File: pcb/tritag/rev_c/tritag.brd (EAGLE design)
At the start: 61 x 34.5 mm, 141 parts, among them J1 BAT_HOLE, J2 CON_MICRO_SDDM3AT-SF-PEJM5, J3 MICRO_USB_B_HIROSE_ZX62-B-5PA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, J4 TC2030-JLINK-NL, J5 TC2030-JLINK-NL, T1 HHM1595A1, U1 DW1000, U10 STM32F091CC, U2 FT232RQ, U3 LIS2DW12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

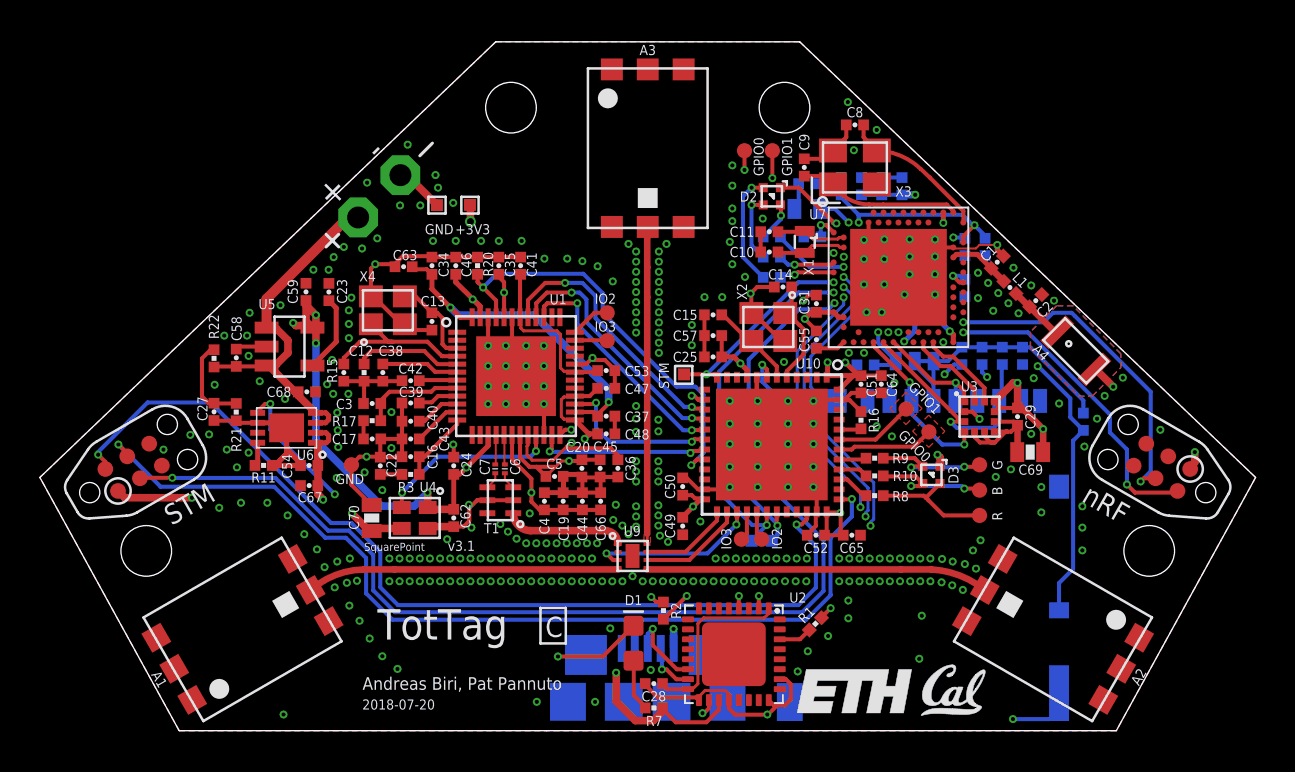
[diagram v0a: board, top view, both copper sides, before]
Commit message: added small fixes from Gerber inspection
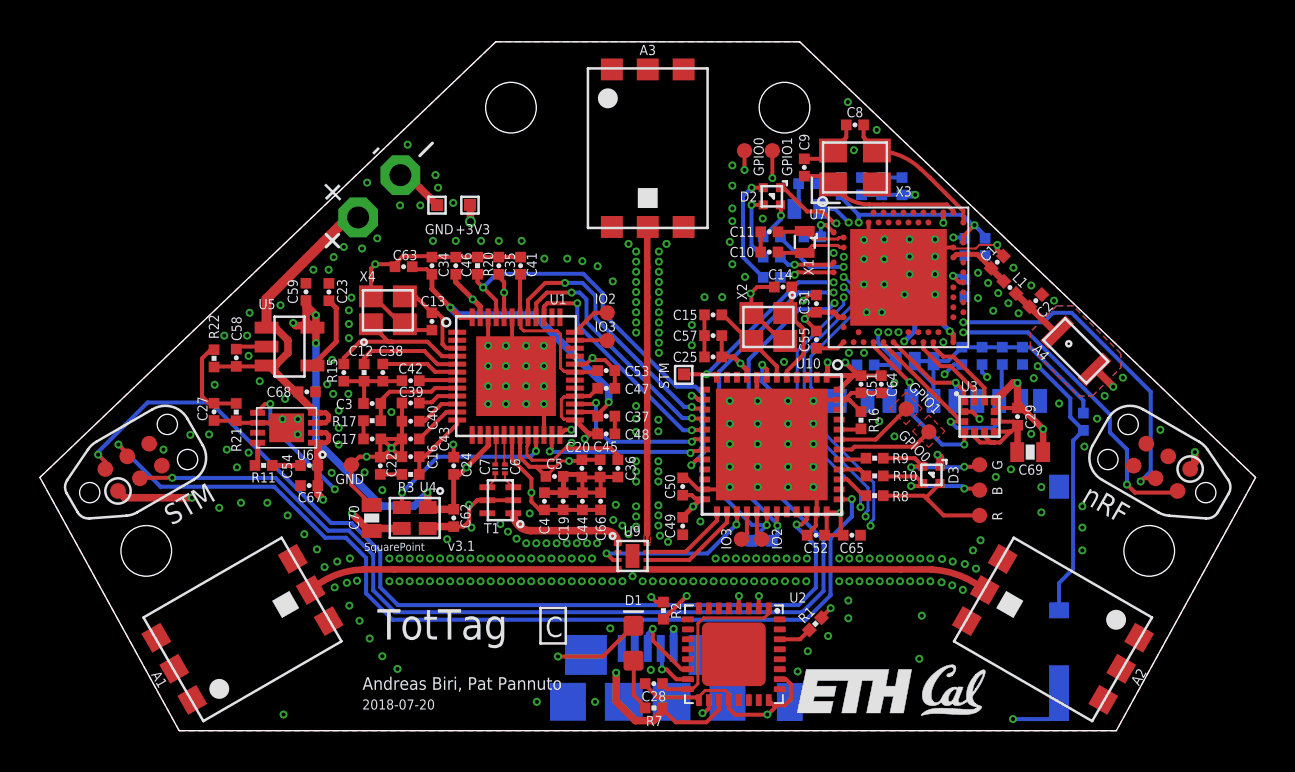
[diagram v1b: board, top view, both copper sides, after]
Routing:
- net GND: track 165.6 -> 166.0 mm, vias 353 -> 356
